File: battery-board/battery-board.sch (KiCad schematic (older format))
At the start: 1 part

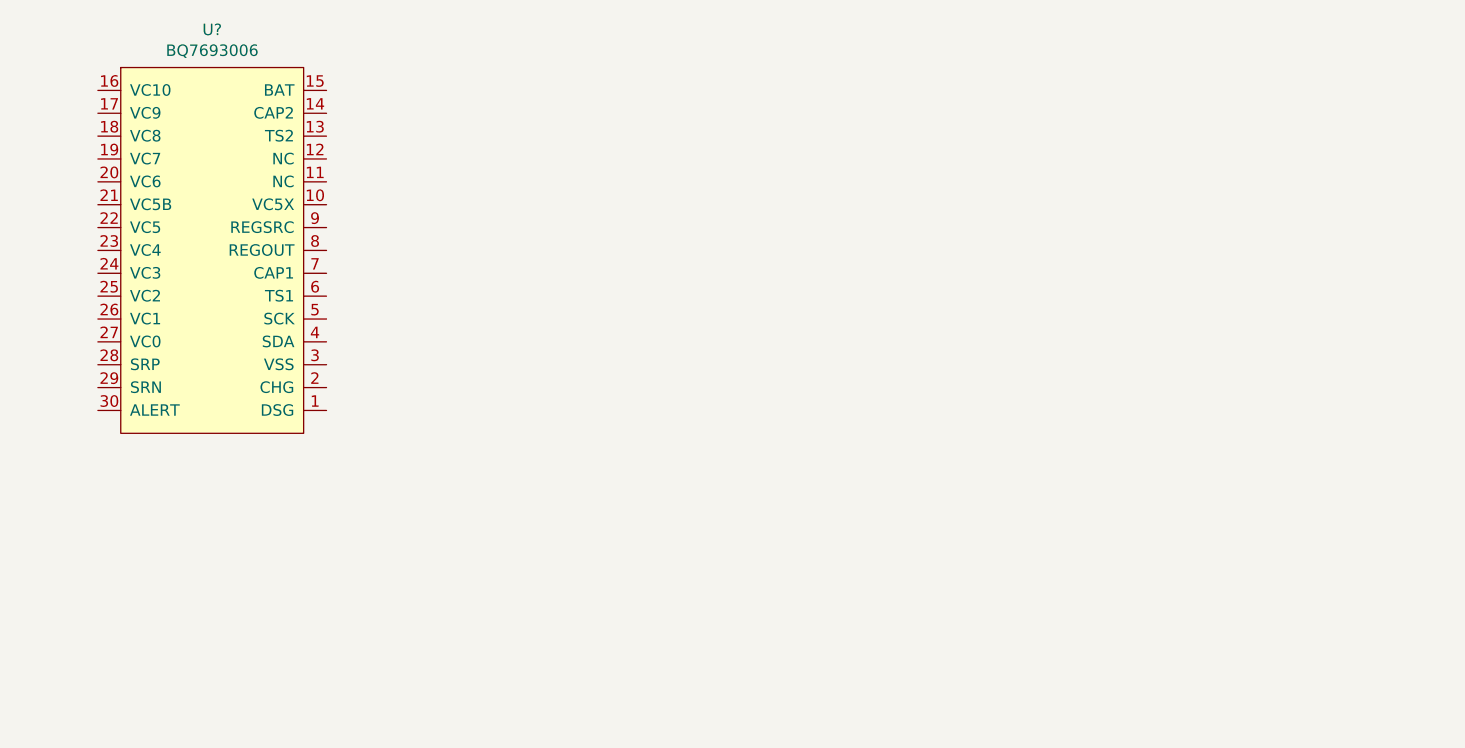
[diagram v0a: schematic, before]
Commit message: removed battery protection (will be implemented off-board)
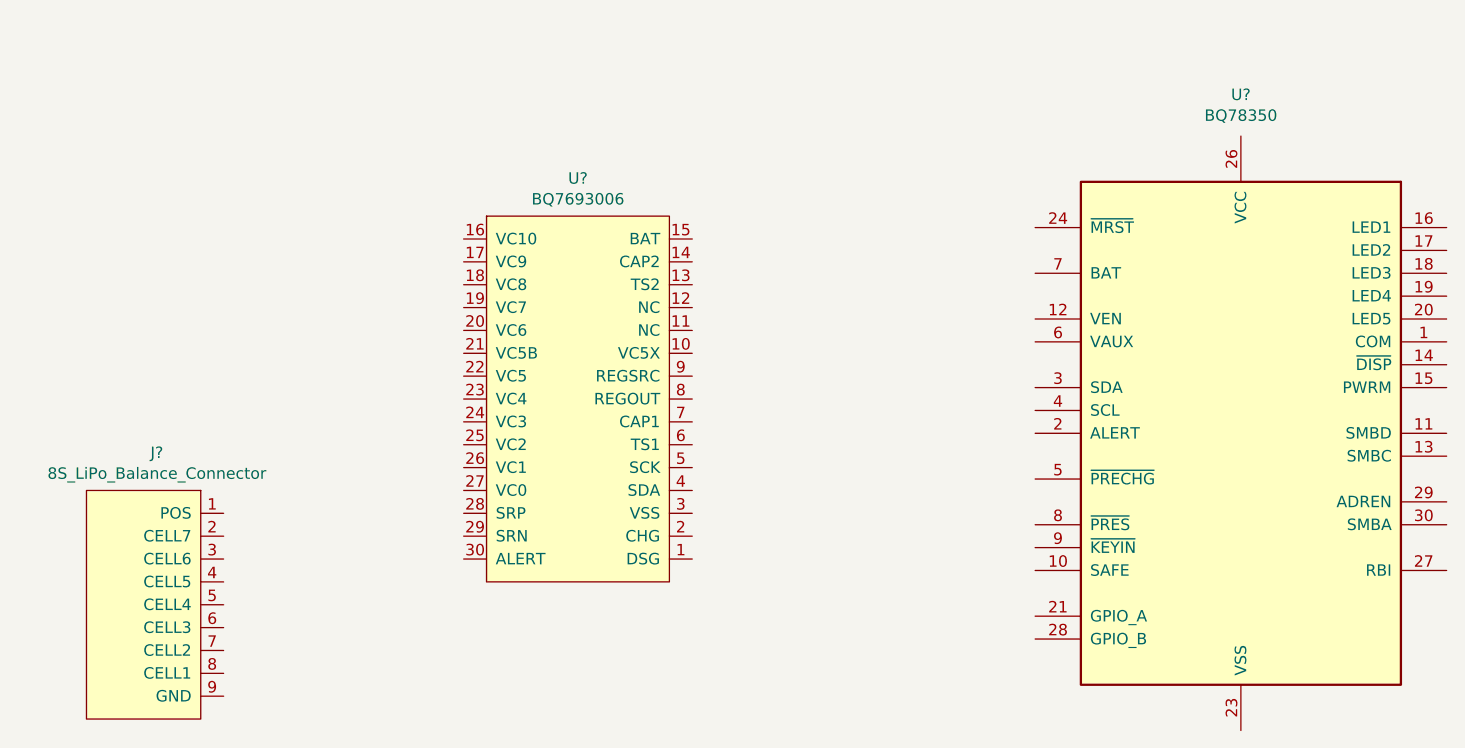
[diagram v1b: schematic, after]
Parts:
- added J?: 8S_LiPo_Balance_Connector, symbol ASTRA_Library:8S_LiPo_Balance_Connector
- added U?: BQ78350, Package_SO:TSSOP-30_4.4x7.8mm_P0.5mm, symbol Battery_Management:BQ78350
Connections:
- new net: U?.22 (VSS), U?.23 (VSS), U?.25 (VSS)
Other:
- moved on the sheet: U?
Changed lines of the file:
@@
 L ASTRA_Library:BQ7693006 U?
 U 1 1 60CE6CB0
-P 1700 2200
-F 0 "U?" H 1700 3115 50  0000 C CNN
-F 1 "BQ7693006" H 1700 3024 50  0000 C CNN
-F 2 "" H 1200 2950 50  0001 C CNN
-F 3 "" H 1200 2950 50  0001 C CNN
-	1    1700 2200
+P 3300 2850
+F 0 "U?" H 3300 3765 50  0000 C CNN
+F 1 "BQ7693006" H 3300 3674 50  0000 C CNN
+F 2 "" H 2800 3600 50  0001 C CNN
+F 3 "" H 2800 3600 50  0001 C CNN
+	1    3300 2850
 	1    0    0    -1
 $EndComp
+$Comp
+L Battery_Management:BQ78350 U?
+U 1 1 60D77019
+P 6200 3050
+F 0 "U?" H 6200 4531 50  0000 C CNN
+F 1 "BQ78350" H 6200 4440 50  0000 C CNN
+F 2 "Package_SO:TSSOP-30_4.4x7.8mm_P0.5mm" H 6200 3050 50  0001 C CNN
+F 3 "http://www.ti.com/lit/ds/symlink/bq78350.pdf" H 5500 4200 50  0001 C CNN
+	1    6200 3050
+	1    0    0    -1
+$EndComp
+$Comp
+L ASTRA_Library:8S_LiPo_Balance_Connector J?
+U 1 1 60D7C55D
+P 1650 3250
+F 0 "J?" H 1842 3365 50  0000 C CNN
+F 1 "8S_LiPo_Balance_Connector" H 1842 3274 50  0000 C CNN
+F 2 "" H 1650 3250 50  0001 C CNN
+F 3 "" H 1650 3250 50  0001 C CNN
+	1    1650 3250
+	-1   0    0    -1
+$EndComp
 $EndSCHEMATC
